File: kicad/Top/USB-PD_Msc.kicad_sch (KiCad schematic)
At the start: 9 parts

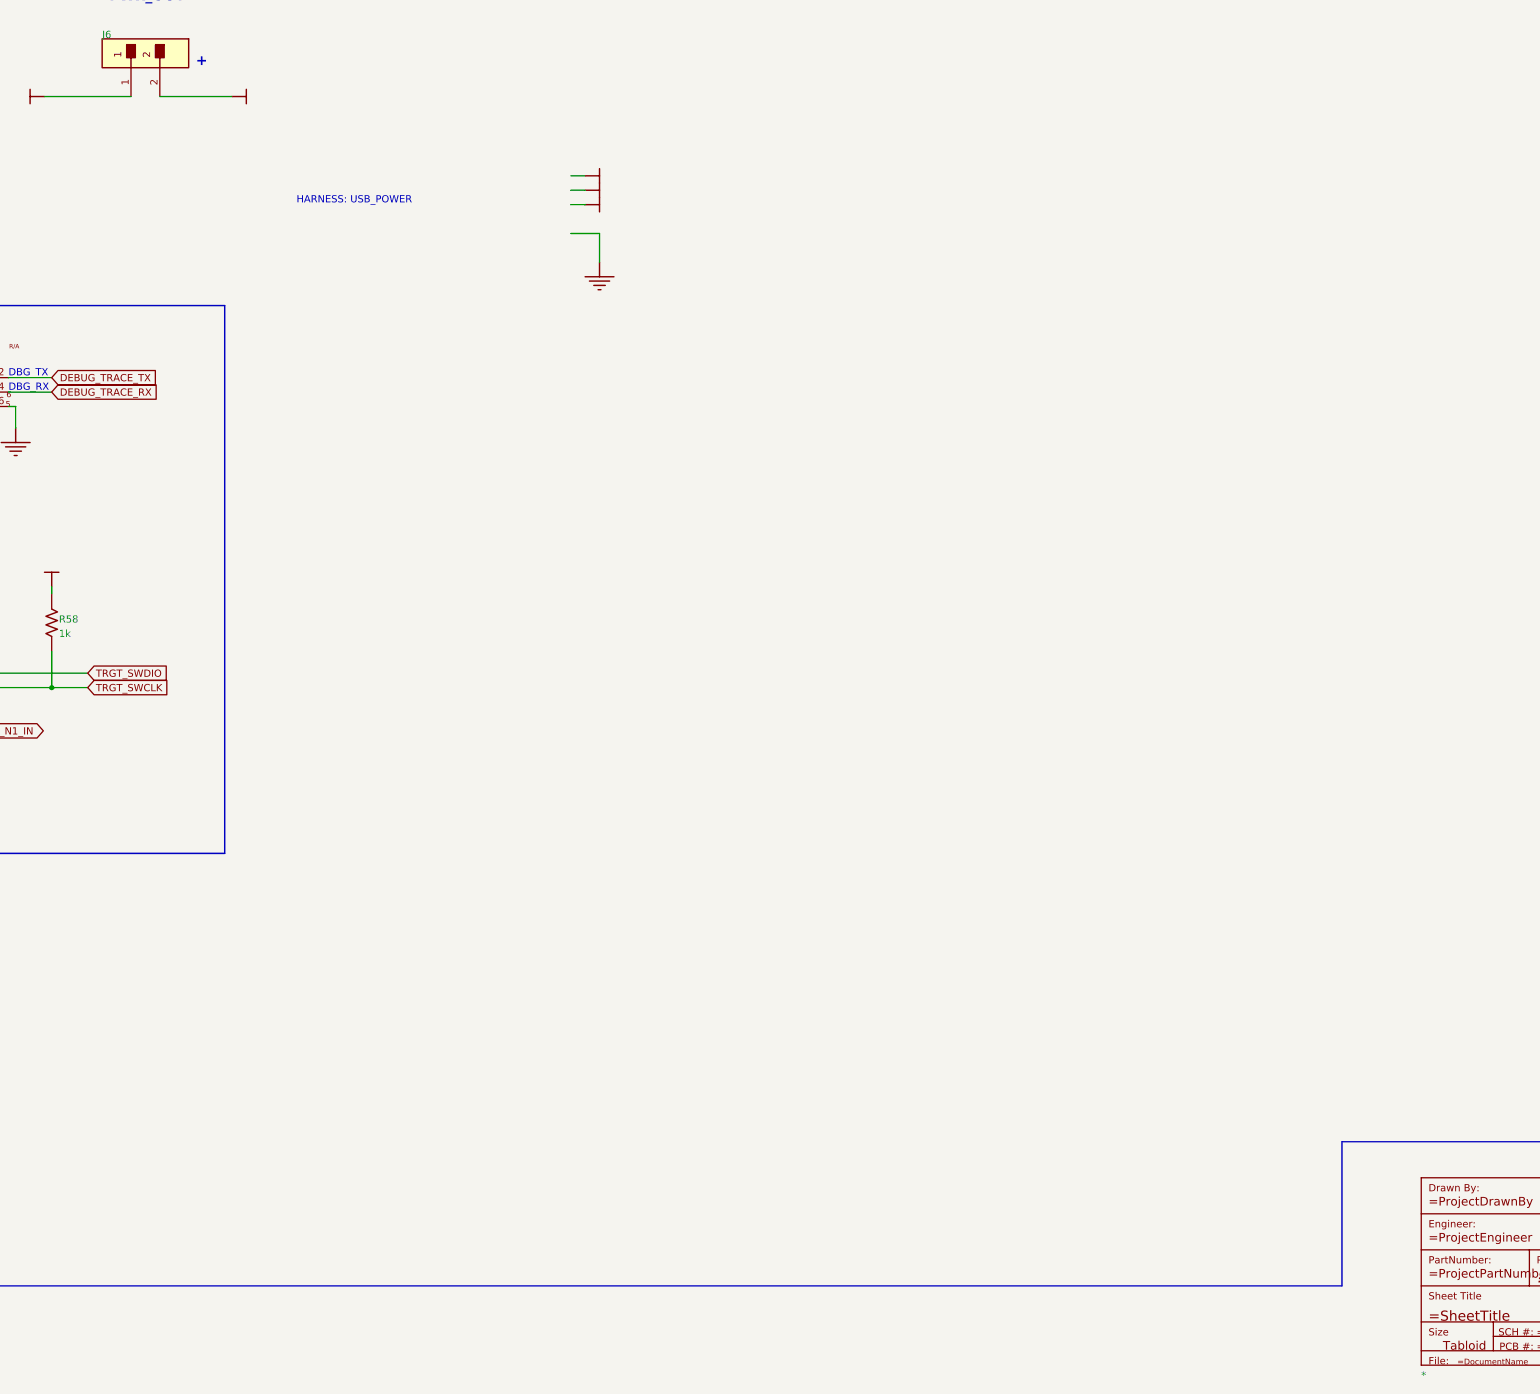
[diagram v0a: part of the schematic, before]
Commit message: Properly synced pcb to schematic
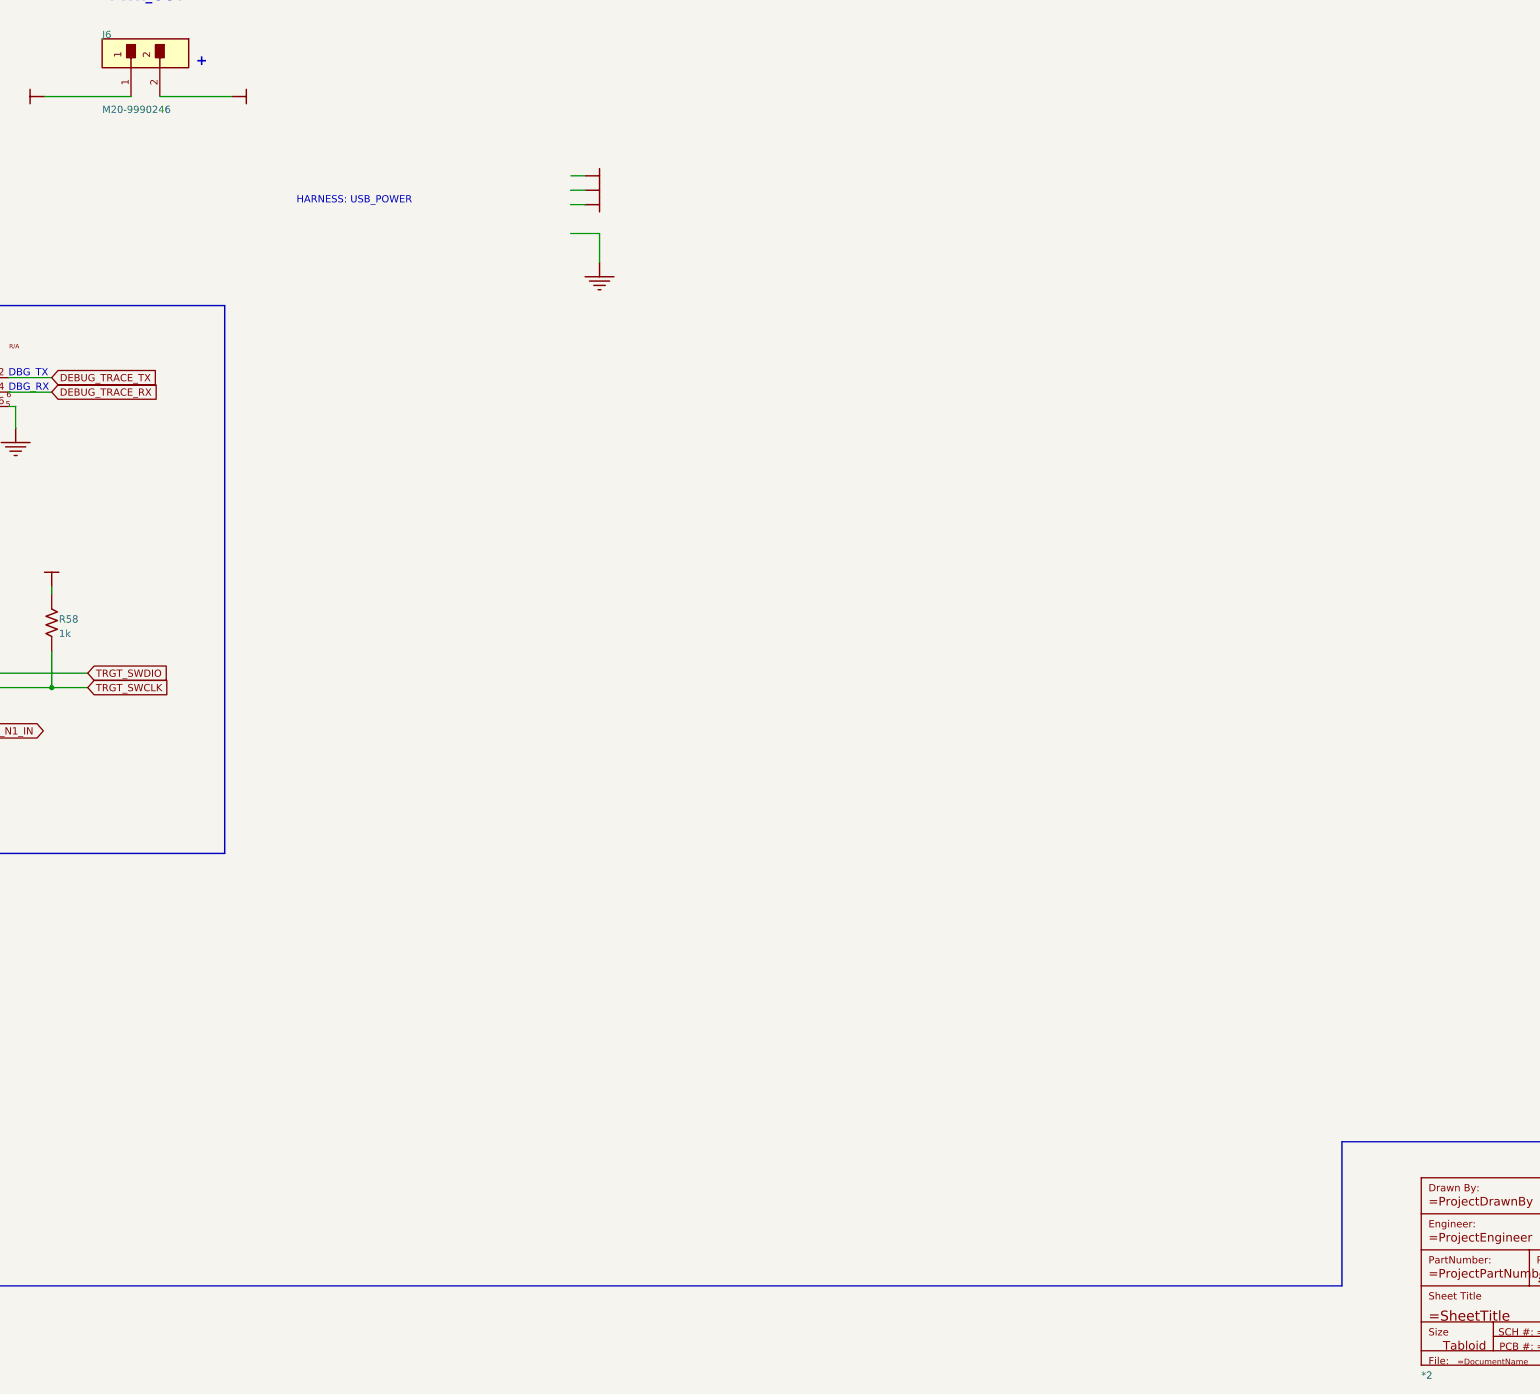
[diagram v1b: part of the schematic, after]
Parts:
- C53: value ~ -> CAP1337; footprint (none) -> AltiumImports:_ALTIUM_WORK_00001_MCHP-CDB_Library_Database_.._Footprints_CAP_C_0402.PcbLib_CAP_C_0402
- J10: value ~ -> Header 2x3; footprint (none) -> AltiumImports:_ALTIUM_WORK_00001_MCHP-CDB_Library_Database_MCHP-CDB.DbLib_Connector_HDR_M_2.54_2x3
- J13: value ~ -> Header 2x5; footprint (none) -> AltiumImports:_ALTIUM_WORK_00001_MCHP-CDB_Library_Database_MCHP-CDB.DbLib_Connector_HDR_M_1.27_2x5_TH_V_FCI_20021111-00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
- J6: value ~ -> M20-9990246; footprint (none) -> AltiumImports:FP-M20-9990246-MFG
- R56: value ~ -> Resistor; footprint (none) -> AltiumImports:_ALTIUM_WORK_00001_MCHP-CDB_Library_Database_MCHP-CDB.DbLib_Resistor_RES_C_0402
- R57, R58: value ~ -> Resistor; footprint (none) -> AltiumImports:_ALTIUM_WORK_00001_MCHP-CDB_Library_Database_.._Footprints_RES_C_0402.PcbLib_RES_C_0402
- TP59: value ~ -> Test Point No BOM; footprint (none) -> AltiumImports:_ALTIUM_WORK_00001_MCHP-CDB_Library_Database_.._Footprints_TP_1mm_SMD.PcbLib_TP_1mm_SMD
- renumbered * to *2
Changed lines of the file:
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@@
   (symbol (lib_id "Top-altium-import:VBUS_USB_OUT") (at 125.73 68.4022 90) (unit 1)
     (in_bom yes) (on_board yes)
-    (property "Reference" "#PWR?" (id 0) (at 125.73 68.4022 0)
+    (property "Reference" "#PWR0150" (id 0) (at 125.73 68.4022 0)
       (effects (font (size 1.27 1.27)) hide)
     )
@@
   (symbol (lib_id "Top-altium-import:3V3_U3") (at 93.98 154.7622 180) (unit 1)
     (in_bom yes) (on_board yes)
-    (property "Reference" "#PWR?" (id 0) (at 93.98 154.7622 0)
+    (property "Reference" "#PWR0143" (id 0) (at 93.98 154.7622 0)
       (effects (font (size 1.27 1.27)) hide)
     )
@@
   (symbol (lib_id "Top-altium-import:VBUS_USB") (at 92.71 68.4022 270) (unit 1)
     (in_bom yes) (on_board yes)
-    (property "Reference" "#PWR?" (id 0) (at 92.71 68.4022 0)
+    (property "Reference" "#PWR0146" (id 0) (at 92.71 68.4022 0)
       (effects (font (size 1.27 1.27)) hide)
     )
@@
   (symbol (lib_id "Top-altium-import:AGND") (at 190.5 97.6122 0) (unit 1)
     (in_bom yes) (on_board yes)
-    (property "Reference" "#PWR?" (id 0) (at 190.5 97.6122 0)
+    (property "Reference" "#PWR0140" (id 0) (at 190.5 97.6122 0)
       (effects (font (size 1.27 1.27)) hide)
     )
@@
   (symbol (lib_id "Top-altium-import:VBUS_USB") (at 187.96 84.9122 90) (unit 1)
     (in_bom yes) (on_board yes)
-    (property "Reference" "#PWR?" (id 0) (at 187.96 84.9122 0)
+    (property "Reference" "#PWR0148" (id 0) (at 187.96 84.9122 0)
       (effects (font (size 1.27 1.27)) hide)
     )
@@
   (symbol (lib_id "Top-altium-import:3V3_U3") (at 22.86 56.9722 180) (unit 1)
     (in_bom yes) (on_board yes)
-    (property "Reference" "#PWR?" (id 0) (at 22.86 56.9722 0)
+    (property "Reference" "#PWR0152" (id 0) (at 22.86 56.9722 0)
       (effects (font (size 1.27 1.27)) hide)
     )
@@
       (effects (font (size 1.27 1.27)) (justify left bottom))
     )
-    (property "Value" "~" (id 1) (at 55.372 167.4622 0)
-      (effects (font (size 1.27 1.27)) (justify left bottom) hide)
-    )
-    (property "Footprint" "" (id 2) (at 66.04 170.0022 0)
+    (property "Value" "Header 2x5" (id 1) (at 55.372 167.4622 0)
+      (effects (font (size 1.27 1.27)) (justify left bottom) hide)
+    )
+    (property "Footprint" "AltiumImports:_ALTIUM_WORK_00001_MCHP-CDB_Library_Database_MCHP-CDB.DbLib_Connector_HDR_M_1.27_2x5_TH_V_FCI_20021111-00010T4LF" (id 2) (at 66.04 170.0022 0)
       (effects (font (size 1.27 1.27)) hide)
     )
@@
   (symbol (lib_id "Top-altium-import:AGND") (at 50.8 180.1622 0) (unit 1)
     (in_bom yes) (on_board yes)
-    (property "Reference" "#PWR?" (id 0) (at 50.8 180.1622 0)
+    (property "Reference" "#PWR0141" (id 0) (at 50.8 180.1622 0)
       (effects (font (size 1.27 1.27)) hide)
     )
@@
   (symbol (lib_id "Top-altium-import:AGND") (at 87.63 126.8222 0) (unit 1)
     (in_bom yes) (on_board yes)
-    (property "Reference" "#PWR?" (id 0) (at 87.63 126.8222 0)
+    (property "Reference" "#PWR0144" (id 0) (at 87.63 126.8222 0)
       (effects (font (size 1.27 1.27)) hide)
     )
@@
   (symbol (lib_id "Top-altium-import:0_Title Block Tabloid") (at 335.28 258.9022 0) (unit 1)
     (in_bom yes) (on_board yes)
-    (property "Reference" "*" (id 0) (at 335.28 294.4622 0)
+    (property "Reference" "*2" (id 0) (at 335.28 294.4622 0)
       (effects (font (size 1.27 1.27)) (justify left bottom))
     )
@@
       (effects (font (size 1.27 1.27)) (justify left bottom))
     )
-    (property "Value" "~" (id 1) (at 21.59 80.5942 0)
-      (effects (font (size 1.27 1.27)) (justify left bottom) hide)
-    )
-    (property "Footprint" "" (id 2) (at 22.86 91.2622 0)
+    (property "Value" "Resistor" (id 1) (at 21.59 80.5942 0)
+      (effects (font (size 1.27 1.27)) (justify left bottom) hide)
+    )
+    (property "Footprint" "AltiumImports:_ALTIUM_WORK_00001_MCHP-CDB_Library_Database_.._Footprints_RES_C_0402.PcbLib_RES_C_0402" (id 2) (at 22.86 91.2622 0)
       (effects (font (size 1.27 1.27)) hide)
     )
@@
   (symbol (lib_id "Top-altium-import:3V3_U3") (at 50.8 167.4622 180) (unit 1)
     (in_bom yes) (on_board yes)
-    (property "Reference" "#PWR?" (id 0) (at 50.8 167.4622 0)
+    (property "Reference" "#PWR0142" (id 0) (at 50.8 167.4622 0)
       (effects (font (size 1.27 1.27)) hide)
     )
@@
       (effects (font (size 1.27 1.27)) (justify left bottom))
     )
-    (property "Value" "~" (id 1) (at 21.59 60.2742 0)
-      (effects (font (size 1.27 1.27)) (justify left bottom) hide)
-    )
-    (property "Footprint" "" (id 2) (at 22.86 70.9422 0)
+    (property "Value" "Resistor" (id 1) (at 21.59 60.2742 0)
+      (effects (font (size 1.27 1.27)) (justify left bottom) hide)
+    )
+    (property "Footprint" "AltiumImports:_ALTIUM_WORK_00001_MCHP-CDB_Library_Database_MCHP-CDB.DbLib_Resistor_RES_C_0402" (id 2) (at 22.86 70.9422 0)
       (effects (font (size 1.27 1.27)) hide)
     )
@@
       (effects (font (size 1.27 1.27)) (justify left bottom))
     )
-    (property "Value" "~" (id 1) (at 92.71 155.5242 0)
-      (effects (font (size 1.27 1.27)) (justify left bottom) hide)
-    )
-    (property "Footprint" "" (id 2) (at 93.98 156.0322 0)
+    (property "Value" "Resistor" (id 1) (at 92.71 155.5242 0)
+      (effects (font (size 1.27 1.27)) (justify left bottom) hide)
+    )
+    (property "Footprint" "AltiumImports:_ALTIUM_WORK_00001_MCHP-CDB_Library_Database_.._Footprints_RES_C_0402.PcbLib_RES_C_0402" (id 2) (at 93.98 156.0322 0)
       (effects (font (size 1.27 1.27)) hide)
     )
@@
       (effects (font (size 1.27 1.27)) (justify left bottom))
     )
-    (property "Value" "~" (id 1) (at 102.87 71.4502 0)
-      (effects (font (size 1.27 1.27)) (justify left bottom))
-    )
-    (property "Footprint" "" (id 2) (at 107.95 68.4022 0)
+    (property "Value" "M20-9990246" (id 1) (at 102.87 71.4502 0)
+      (effects (font (size 1.27 1.27)) (justify left bottom))
+    )
+    (property "Footprint" "AltiumImports:FP-M20-9990246-MFG" (id 2) (at 107.95 68.4022 0)
       (effects (font (size 1.27 1.27)) hide)
     )
@@
       (effects (font (size 1.27 1.27)) (justify left bottom))
     )
-    (property "Value" "~" (id 1) (at 71.628 180.9242 0)
-      (effects (font (size 1.27 1.27)) (justify left bottom) hide)
-    )
-    (property "Footprint" "" (id 2) (at 73.66 181.4322 0)
+    (property "Value" "CAP1337" (id 1) (at 71.628 180.9242 0)
+      (effects (font (size 1.27 1.27)) (justify left bottom) hide)
+    )
+    (property "Footprint" "AltiumImports:_ALTIUM_WORK_00001_MCHP-CDB_Library_Database_.._Footprints_CAP_C_0402.PcbLib_CAP_C_0402" (id 2) (at 73.66 181.4322 0)
       (effects (font (size 1.27 1.27)) hide)
     )
@@
       (effects (font (size 1.27 1.27)) (justify left bottom))
     )
-    (property "Value" "~" (id 1) (at 77.47 120.4722 0)
-      (effects (font (size 1.27 1.27)) (justify left bottom) hide)
-    )
-    (property "Footprint" "" (id 2) (at 78.74 116.6622 0)
+    (property "Value" "Header 2x3" (id 1) (at 77.47 120.4722 0)
+      (effects (font (size 1.27 1.27)) (justify left bottom) hide)
+    )
+    (property "Footprint" "AltiumImports:_ALTIUM_WORK_00001_MCHP-CDB_Library_Database_MCHP-CDB.DbLib_Connector_HDR_M_2.54_2x3" (id 2) (at 78.74 116.6622 0)
       (effects (font (size 1.27 1.27)) hide)
     )
@@
   (symbol (lib_id "Top-altium-import:3V3_U3") (at 187.96 87.4522 90) (unit 1)
     (in_bom yes) (on_board yes)
-    (property "Reference" "#PWR?" (id 0) (at 187.96 87.4522 0)
+    (property "Reference" "#PWR0147" (id 0) (at 187.96 87.4522 0)
       (effects (font (size 1.27 1.27)) hide)
     )
@@
   (symbol (lib_id "Top-altium-import:AGND") (at 73.66 192.8622 0) (unit 1)
     (in_bom yes) (on_board yes)
-    (property "Reference" "#PWR?" (id 0) (at 73.66 192.8622 0)
+    (property "Reference" "#PWR0145" (id 0) (at 73.66 192.8622 0)
       (effects (font (size 1.27 1.27)) hide)
     )
@@
   (symbol (lib_id "Top-altium-import:AGND") (at 22.86 93.8022 0) (unit 1)
     (in_bom yes) (on_board yes)
-    (property "Reference" "#PWR?" (id 0) (at 22.86 93.8022 0)
+    (property "Reference" "#PWR0151" (id 0) (at 22.86 93.8022 0)
       (effects (font (size 1.27 1.27)) hide)
     )
@@
       (effects (font (size 1.27 1.27)) (justify left bottom))
     )
-    (property "Value" "~" (id 1) (at 38.1 74.7522 90)
-      (effects (font (size 1.27 1.27)) hide)
-    )
-    (property "Footprint" "" (id 2) (at 35.56 77.2922 0)
+    (property "Value" "Test Point No BOM" (id 1) (at 38.1 74.7522 90)
+      (effects (font (size 1.27 1.27)) hide)
+    )
+    (property "Footprint" "AltiumImports:_ALTIUM_WORK_00001_MCHP-CDB_Library_Database_.._Footprints_TP_1mm_SMD.PcbLib_TP_1mm_SMD" (id 2) (at 35.56 77.2922 0)
       (effects (font (size 1.27 1.27)) hide)
     )
@@
   (symbol (lib_id "Top-altium-import:VBUS_USB_OUT") (at 187.96 82.3722 90) (unit 1)
     (in_bom yes) (on_board yes)
-    (property "Reference" "#PWR?" (id 0) (at 187.96 82.3722 0)
-      (effects (font (size 1.27 1.27)) hide)
-    )
+    (property "Reference" "#PWR0149" (id 0) (at 187.96 82.3722 0)
+      (effects (font (size 1.27 1.27)) hide)
+    )
